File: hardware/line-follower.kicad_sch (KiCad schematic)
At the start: 40 parts, among them U1 QRE1113GR, U10 QRE1113GR, U2 QRE1113GR, U3 QRE1113GR, U4 QRE1113GR, U5 QRE1113GR, U6 QRE1113GR, U7 QRE1113GR, U8 QRE1113GR, U9 QRE1113GR

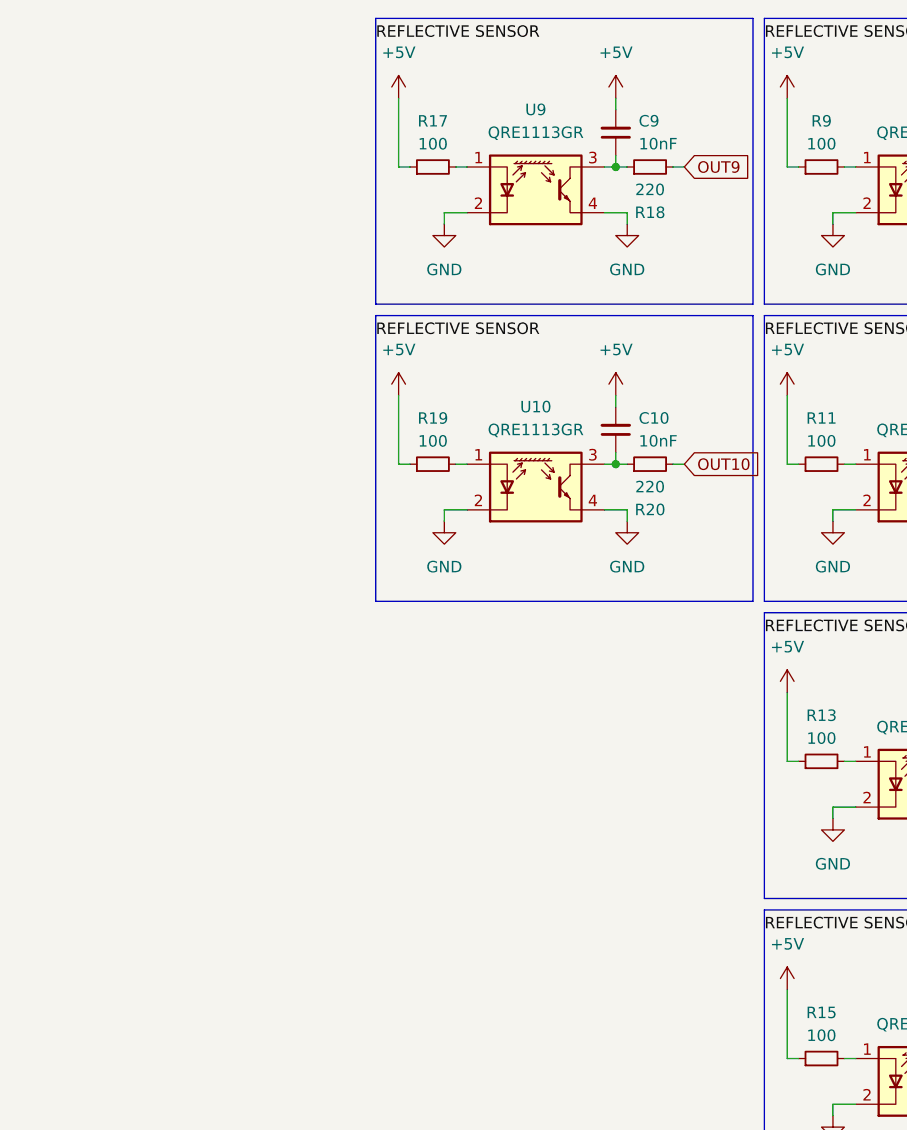
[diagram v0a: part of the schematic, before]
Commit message: array wiring
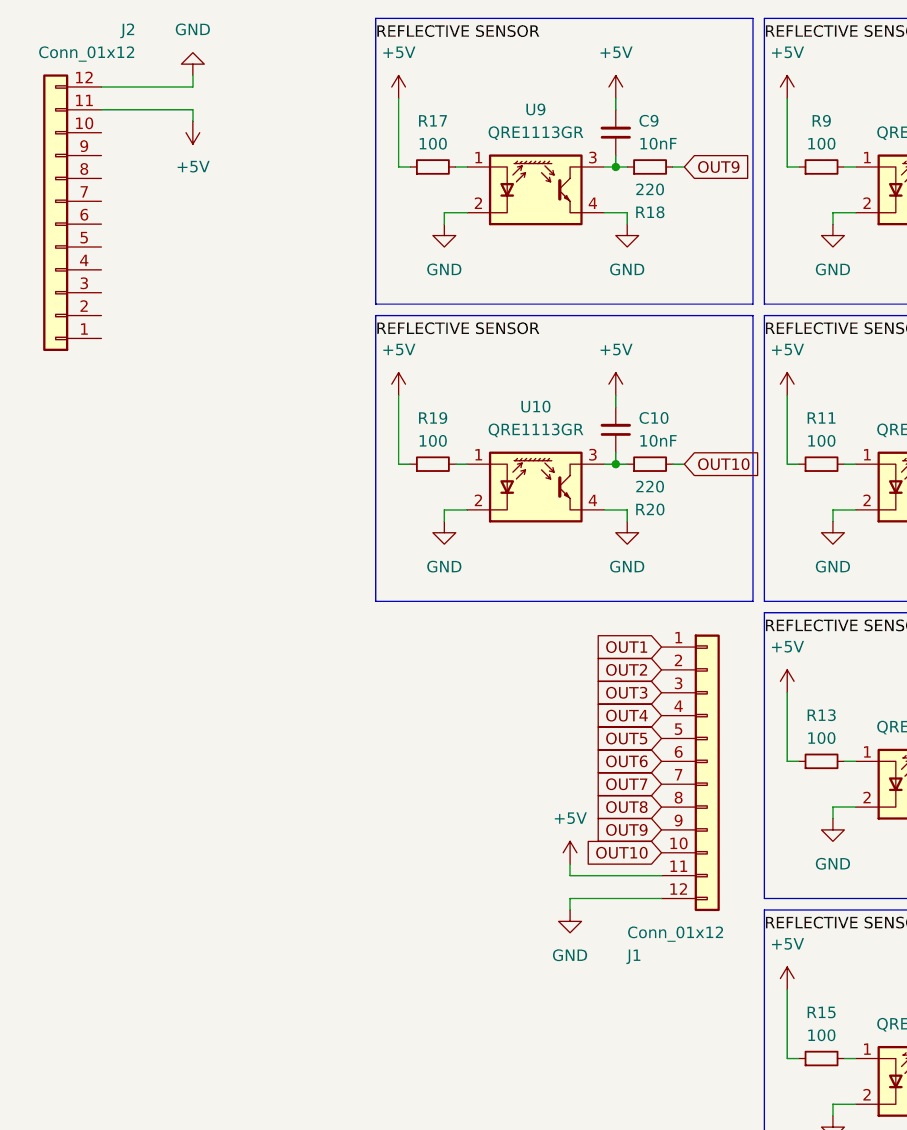
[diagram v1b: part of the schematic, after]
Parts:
- added J1, J2: Conn_01x12, Connector_Molex:Molex_PicoBlade_53047-1210_1x12_P1.25mm_Vertical, symbol Connector_Generic:Conn_01x12
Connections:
- net +5V: now also J1.11 (Pin_11), J2.11 (Pin_11)
- net GND: now also J1.12 (Pin_12), J2.12 (Pin_12)
- net OUT1: now also J1.1 (Pin_1)
- net OUT10: now also J1.10 (Pin_10)
- net OUT2: now also J1.2 (Pin_2)
- net OUT3: now also J1.3 (Pin_3)
- net OUT4: now also J1.4 (Pin_4)
- net OUT5: now also J1.5 (Pin_5)
- net OUT6: now also J1.6 (Pin_6)
- net OUT7: now also J1.7 (Pin_7)
- net OUT8: now also J1.8 (Pin_8)
- net OUT9: now also J1.9 (Pin_9)

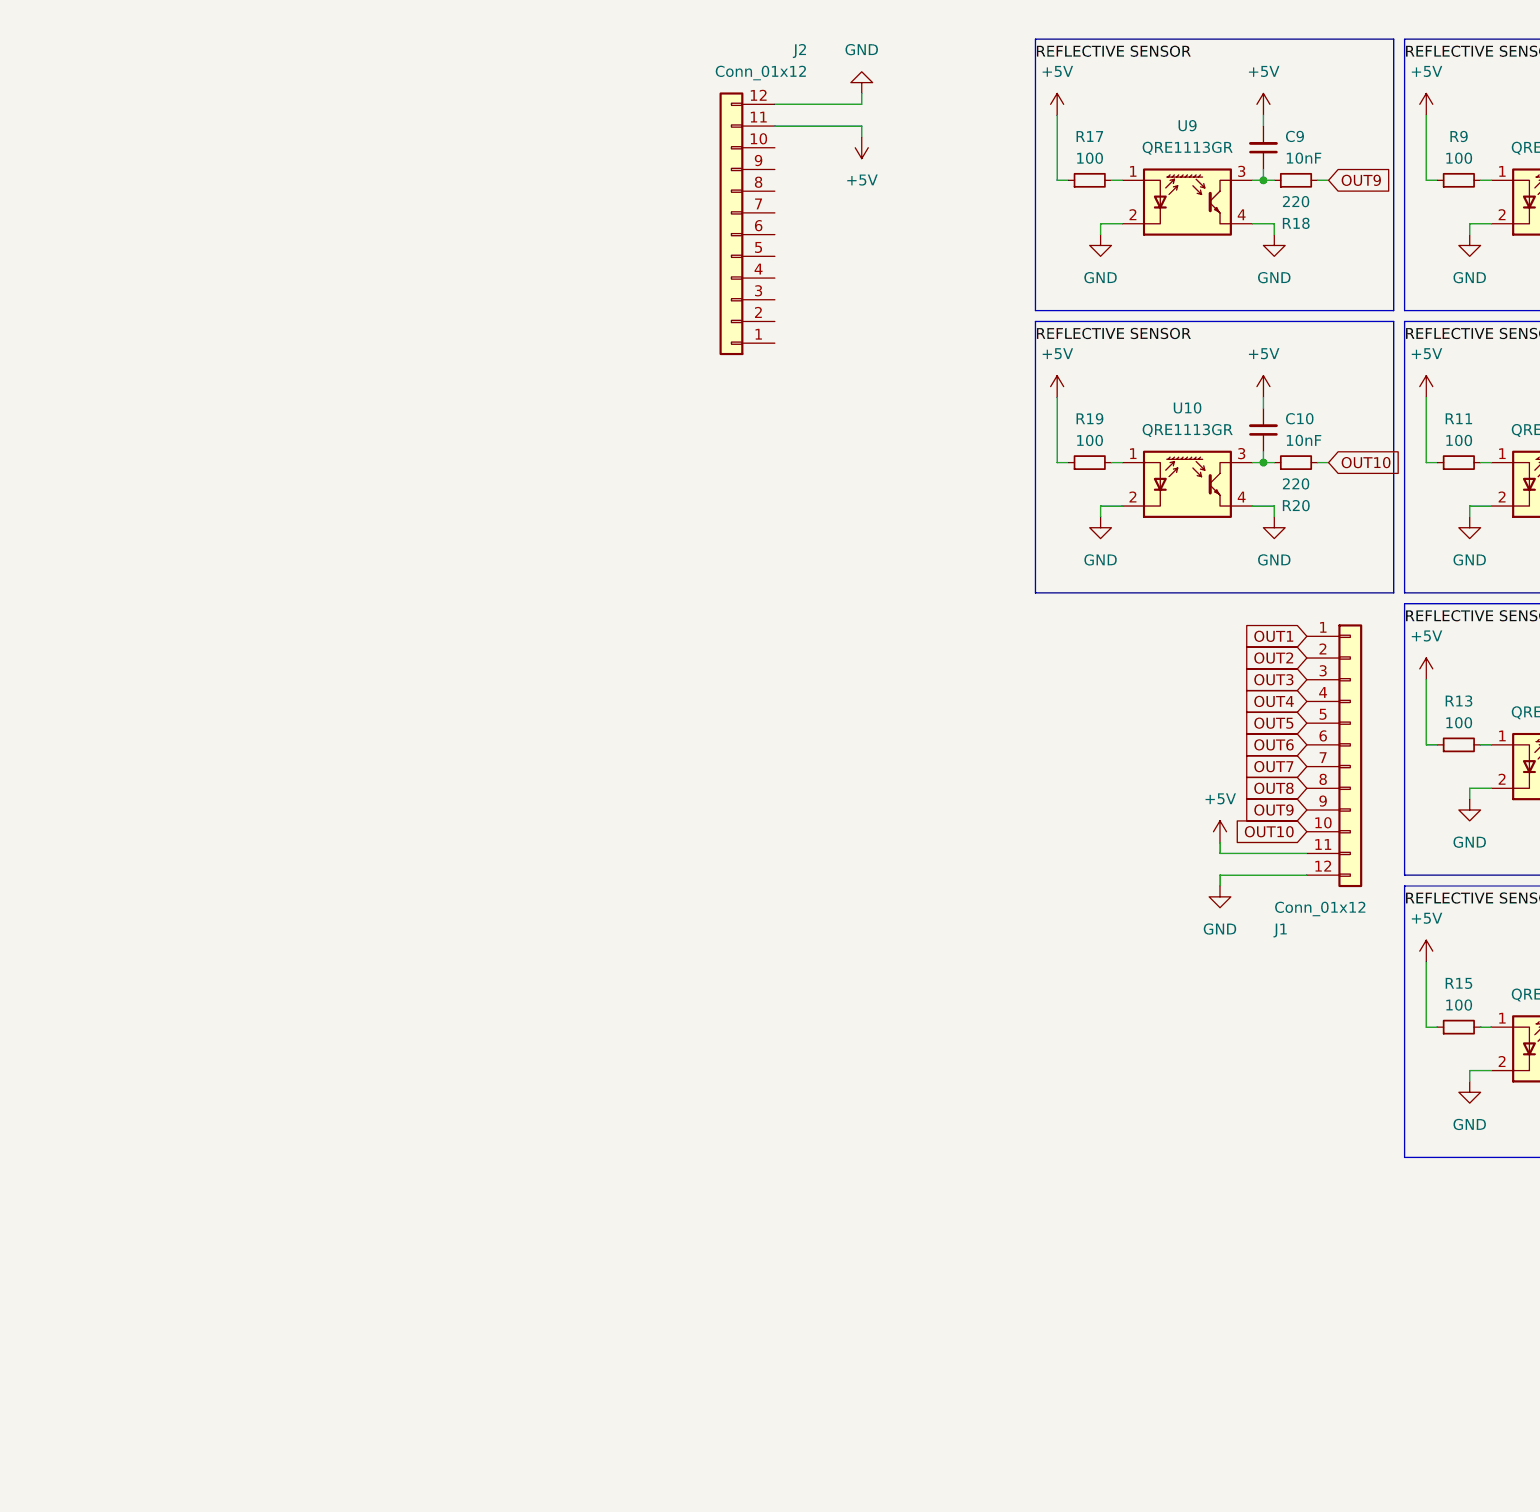
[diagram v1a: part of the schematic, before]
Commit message: add mcu
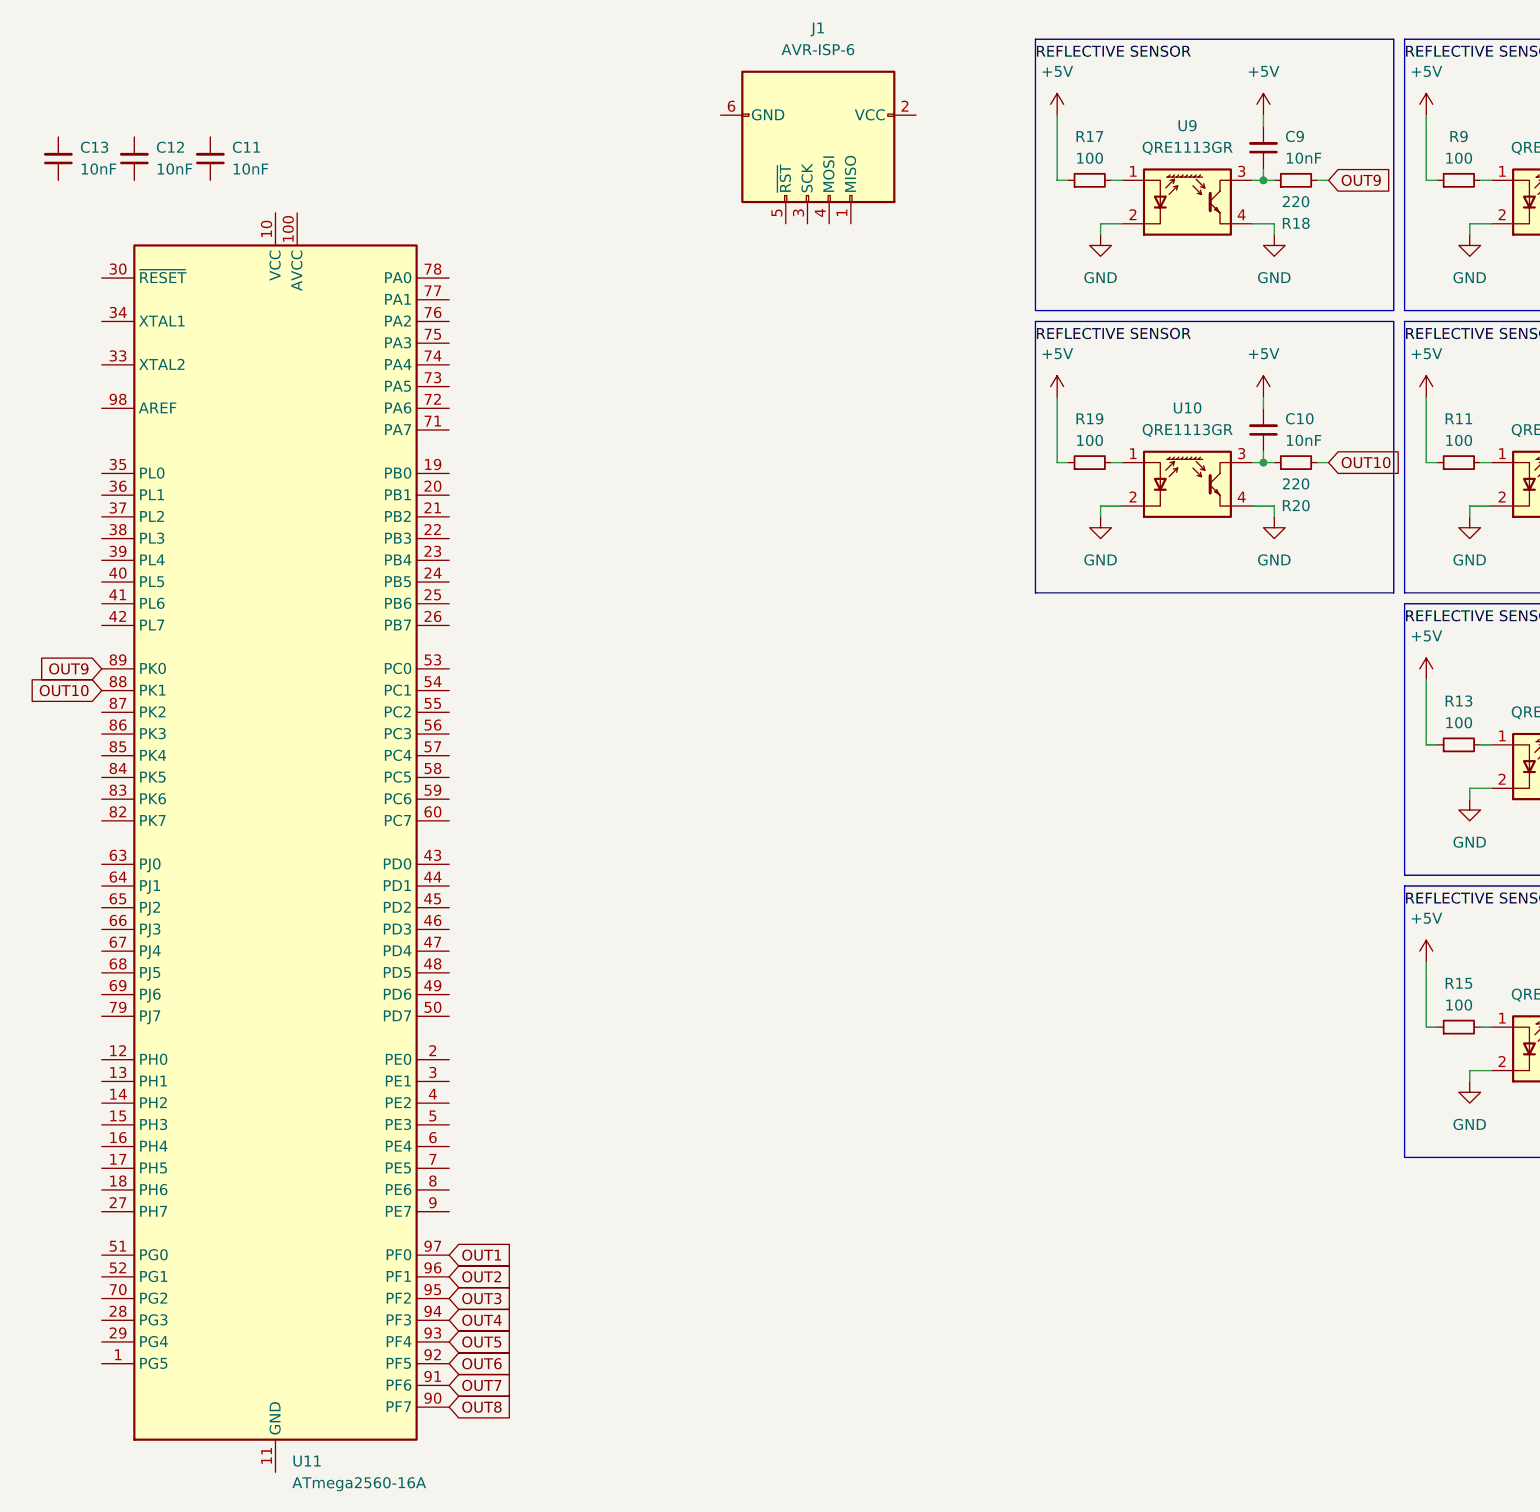
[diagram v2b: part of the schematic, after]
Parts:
- removed J1, J2: Conn_01x12, Connector_Molex:Molex_PicoBlade_53047-1210_1x12_P1.25mm_Vertical, symbol Connector_Generic:Conn_01x12
- added C11, C12, C13: 10nF, Capacitor_SMD:C_0603_1608Metric, symbol Device:C_Small
- added J1: AVR-ISP-6, symbol Connector:AVR-ISP-6
- added U11: ATmega2560-16A, Package_QFP:TQFP-100_14x14mm_P0.5mm, symbol MCU_Microchip_ATmega:ATmega2560-16A
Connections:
- net OUT1: now also U11.97 (PF0)
- net OUT10: now also U11.88 (PK1)
- net OUT2: now also U11.96 (PF1)
- net OUT3: now also U11.95 (PF2)
- net OUT4: now also U11.94 (PF3)
- net OUT5: now also U11.93 (PF4)
- net OUT6: now also U11.92 (PF5)
- net OUT7: now also U11.91 (PF6)
- net OUT8: now also U11.90 (PF7)
- net OUT9: now also U11.89 (PK0)
- new net: U11.10 (VCC), U11.31 (VCC), U11.61 (VCC), U11.80 (VCC)
- new net: U11.11 (GND), U11.32 (GND), U11.62 (GND), U11.81 (GND), U11.99 (GND)
